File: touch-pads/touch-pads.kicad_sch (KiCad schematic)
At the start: 47 parts, among them J1 Conn_01x06_Pin, J2 Conn_01x06_Socket, J3 Conn_01x06_Pin, K1 Conn_01x01, K10 Conn_01x01, K11 Conn_01x01, K12 Conn_01x01, K13 Conn_01x01, K14 Conn_01x01, K15 Conn_01x01, K16 Conn_01x01, K17 Conn_01x01, K18 Conn_01x01, K19 Conn_01x01, K2 Conn_01x01, K20 Conn_01x01, K21 Conn_01x01, K22 Conn_01x01, K23 Conn_01x01, K24 Conn_01x01, K25 Conn_01x01, K26 Conn_01x01, K27 Conn_01x01, K28 Conn_01x01, K29 Conn_01x01, K3 Conn_01x01, K30 Conn_01x01, K31 Conn_01x01, K32 Conn_01x01, K4 Conn_01x01, K5 Conn_01x01, K6 Conn_01x01, K7 Conn_01x01, K8 Conn_01x01, K9 Conn_01x01, U10 CAP1188-1-CP-TR, U11 CAP1188-1-CP-TR, U8 CAP1188-1-CP-TR, U9 CAP1188-1-CP-TR

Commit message: small board
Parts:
- removed K10, K11, K12, K13, K14, K15, K16, K17, K18, K19, K20, K21, K22, K23, K24, K25, K26, K27, K28, K29, K30, K31, K32, K9: Conn_01x01, TouchKey:TouchKey_Standard, symbol Connector_Generic:Conn_01x01
- removed R16, R17, R18: 10k, Resistor_SMD:R_0805_2012Metric_Pad1.20x1.40mm_HandSolder, symbol Device:R
- removed R20: 120k, Resistor_SMD:R_0805_2012Metric_Pad1.20x1.40mm_HandSolder, symbol Device:R
- removed R21: 100k, Resistor_SMD:R_0805_2012Metric_Pad1.20x1.40mm_HandSolder, symbol Device:R
- removed R22: 82k, Resistor_SMD:R_0805_2012Metric_Pad1.20x1.40mm_HandSolder, symbol Device:R
- removed U10, U11, U9: CAP1188-1-CP-TR, CAP1188_1_CP_TR:QFN24_4X4MC_MCH, symbol CAP1188_1_CP_TR:CAP1188-1-CP-TR
- J1, J3: footprint (none) -> Connector_PinHeader_2.54mm:PinHeader_1x06_P2.54mm_Horizontal
- J2: footprint (none) -> Connector_PinSocket_2.54mm:PinSocket_1x06_P2.54mm_Horizontal
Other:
- moved on the sheet: J1, J2, J3, K1, K2, K3, K4, K5, K6, K7, K8, R15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

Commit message: large board
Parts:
- removed J1, J3: Conn_01x06_Pin, Connector_PinHeader_2.54mm:PinHeader_1x06_P2.54mm_Horizontal, symbol Connector:Conn_01x06_Pin
- added K10, K11, K12, K13, K14, K15, K16, K17, K18, K19, K20, K21, K22, K23, K24, K25, K26, K27, K28, K29, K30, K31, K32, K9: Conn_01x01, TouchKey:TouchKey_Standard, symbol Connector_Generic:Conn_01x01
- added R2, R5, R6: 10k, Resistor_SMD:R_0805_2012Metric_Pad1.20x1.40mm_HandSolder, symbol Device:R
- added R4: 100k, Resistor_SMD:R_0805_2012Metric_Pad1.20x1.40mm_HandSolder, symbol Device:R
- added R7: 120k, Resistor_SMD:R_0805_2012Metric_Pad1.20x1.40mm_HandSolder, symbol Device:R
- added R8: 82k, Resistor_SMD:R_0805_2012Metric_Pad1.20x1.40mm_HandSolder, symbol Device:R
- added U2, U3, U4: CAP1188-1-CP-TR, CAP1188_1_CP_TR:QFN24_4X4MC_MCH, symbol CAP1188_1_CP_TR:CAP1188-1-CP-TR
- J1: renamed from J2; footprint Connector_PinSocket_2.54mm:PinSocket_1x06_P2.54mm_Horizontal -> Connector_JST:JST_XH_B6B-XH-A_1x06_P2.50mm_Vertical
- renumbered R15 to R1, R19 to R3, U8 to U1
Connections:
- net +3.3V: now also J1.4 (Pin_4), U2.23 (VDD), U3.23 (VDD), U4.23 (VDD); no longer J1.5 (Pin_5)
- net ALERT: now also J1.6 (Pin_6), U2.13 (*ALERT/*BC_IRQ), U3.13 (*ALERT/*BC_IRQ), U4.13 (*ALERT/*BC_IRQ); no longer J1.1 (Pin_1)
- net GND: now also J1.5 (Pin_5), R2.1, R4.2, R5.1, R6.1, R7.2, R8.2, U2.1 (*SPI_CS), U2.10 (LED6), U2.11 (LED7), U2.12 (LED8), U2.25 (EPAD), U2.5 (LED1), U2.6 (LED2), U2.7 (LED3), U2.8 (LED4), U2.9 (LED5), U3.1 (*SPI_CS), U3.10 (LED6), U3.11 (LED7), U3.12 (LED8), U3.25 (EPAD), U3.5 (LED1), U3.6 (LED2), U3.7 (LED3), U3.8 (LED4), U3.9 (LED5), U4.1 (*SPI_CS), U4.10 (LED6), U4.11 (LED7), U4.12 (LED8), U4.25 (EPAD), U4.5 (LED1), U4.6 (LED2), U4.7 (LED3), U4.8 (LED4), U4.9 (LED5); no longer J1.6 (Pin_6)
- net RESET: now also J1.3 (Pin_3), U2.24 (RESET), U3.24 (RESET), U4.24 (RESET); no longer J1.2 (Pin_2)
- net SMCLK: now also J1.1 (Pin_1), U2.4 (SMCLK/BC_CLK/SPI_CLK), U3.4 (SMCLK/BC_CLK/SPI_CLK), U4.4 (SMCLK/BC_CLK/SPI_CLK); no longer J1.4 (Pin_4)
- net SMDATA: now also J1.2 (Pin_2), U2.3 (SMDATA/BC_DATA/SPI_MSIO/SPI_MISO), U3.3 (SMDATA/BC_DATA/SPI_MSIO/SPI_MISO), U4.3 (SMDATA/BC_DATA/SPI_MSIO/SPI_MISO); no longer J1.3 (Pin_3)
- new net: K19.1 (Pin_1), U2.20 (CS3)
- new net: K12.1 (Pin_1), U3.19 (CS4)
- new net: R6.2, U4.2 (WAKE/SPI_MOSI)
- new net: K13.1 (Pin_1), U3.18 (CS5)
- new net: K29.1 (Pin_1), U4.18 (CS5)
- new net: K25.1 (Pin_1), U4.22 (CS1)
- new net: K14.1 (Pin_1), U3.17 (CS6)
- new net: R7.1, U3.14 (ADDR_COMM)
- new net: K16.1 (Pin_1), U3.15 (CS8)
- new net: K15.1 (Pin_1), U3.16 (CS7)
- new net: R5.2, U3.2 (WAKE/SPI_MOSI)
- new net: K11.1 (Pin_1), U3.20 (CS3)
- new net: K10.1 (Pin_1), U3.21 (CS2)
- new net: K9.1 (Pin_1), U3.22 (CS1)
- new net: K21.1 (Pin_1), U2.18 (CS5)
- new net: R2.2, U2.2 (WAKE/SPI_MOSI)
- new net: K31.1 (Pin_1), U4.16 (CS7)
- new net: K23.1 (Pin_1), U2.16 (CS7)
- new net: K32.1 (Pin_1), U4.15 (CS8)
- new net: R8.1, U4.14 (ADDR_COMM)
- new net: K30.1 (Pin_1), U4.17 (CS6)
- new net: K28.1 (Pin_1), U4.19 (CS4)
- new net: K27.1 (Pin_1), U4.20 (CS3)
- new net: K26.1 (Pin_1), U4.21 (CS2)
- new net: K17.1 (Pin_1), U2.22 (CS1)
- new net: K22.1 (Pin_1), U2.17 (CS6)
- new net: R4.1, U2.14 (ADDR_COMM)
- new net: K24.1 (Pin_1), U2.15 (CS8)
- new net: K20.1 (Pin_1), U2.19 (CS4)
- new net: K18.1 (Pin_1), U2.21 (CS2)
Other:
- moved on the sheet: J1

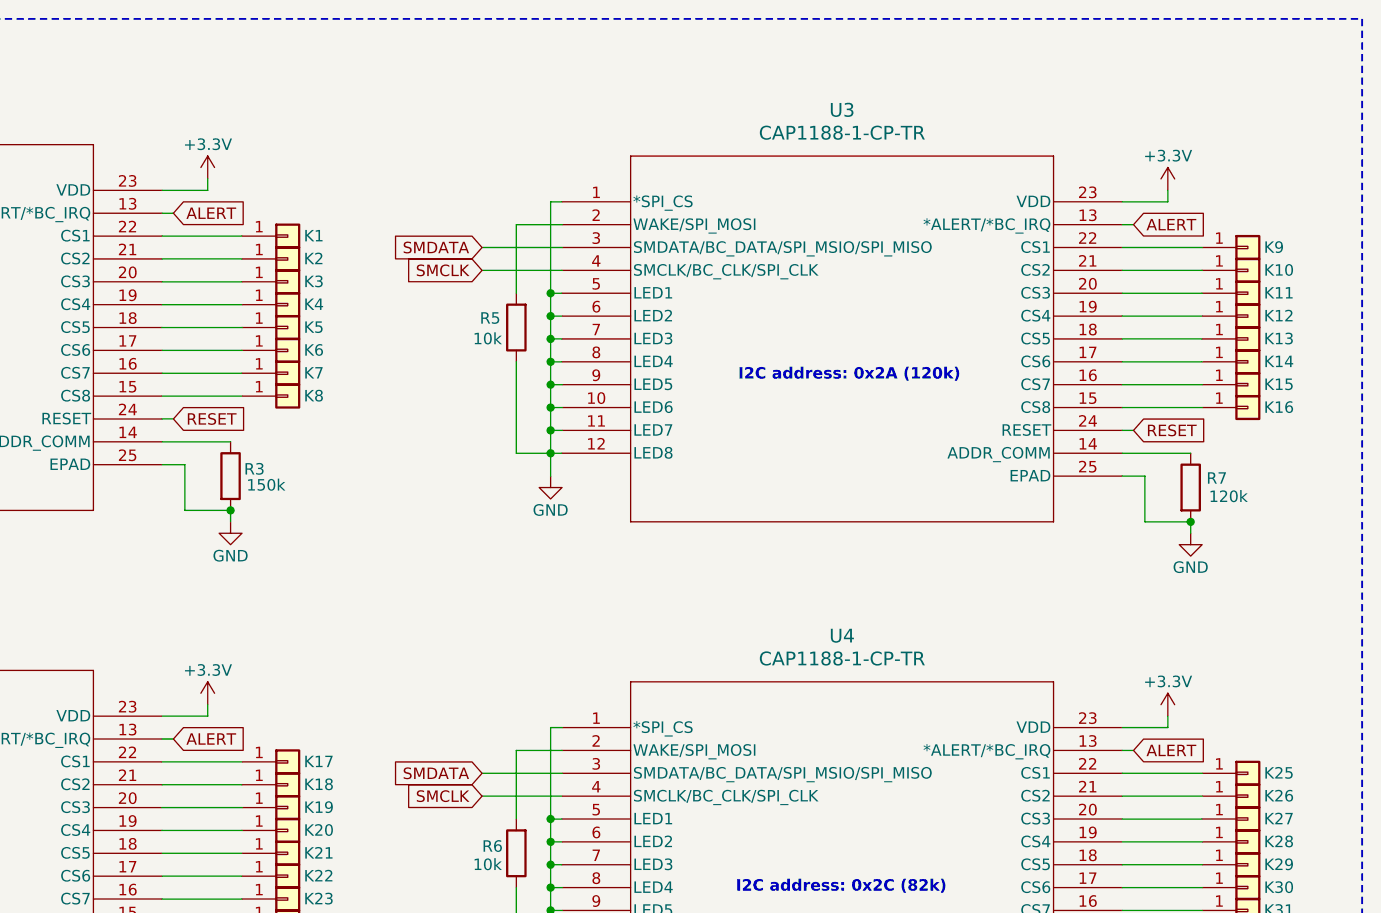
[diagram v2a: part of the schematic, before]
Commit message: add bypass caps
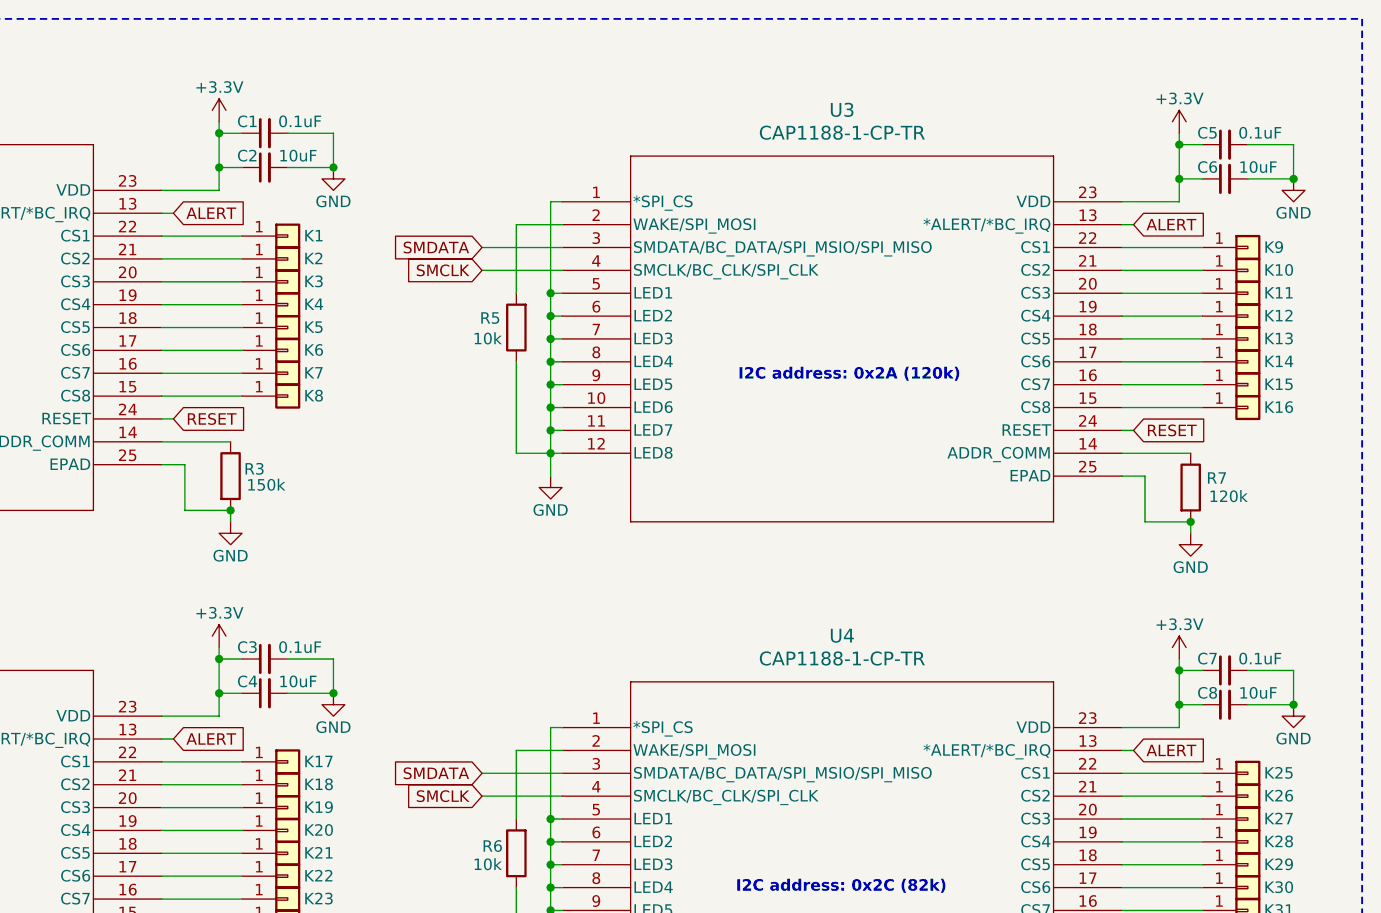
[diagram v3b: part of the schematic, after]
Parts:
- added C1, C3, C5, C7: 0.1uF, Capacitor_SMD:C_0805_2012Metric_Pad1.18x1.45mm_HandSolder, symbol Device:C_Small
- added C2, C4, C6, C8: 10uF, Capacitor_SMD:C_0805_2012Metric_Pad1.18x1.45mm_HandSolder, symbol Device:C_Small
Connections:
- net +3.3V: now also C1.1, C2.1, C3.1, C4.1, C5.1, C6.1, C7.1, C8.1
- net GND: now also C1.2, C2.2, C3.2, C4.2, C5.2, C6.2, C7.2, C8.2

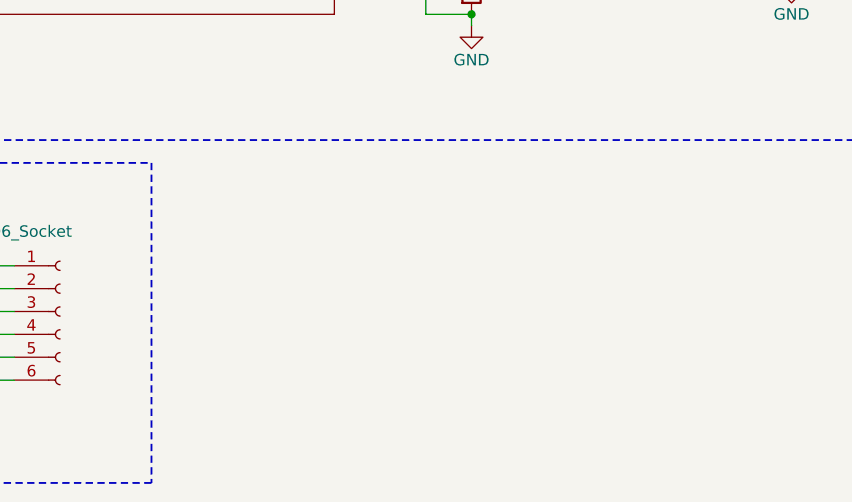
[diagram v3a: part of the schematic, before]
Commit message: mounting holes on schematic
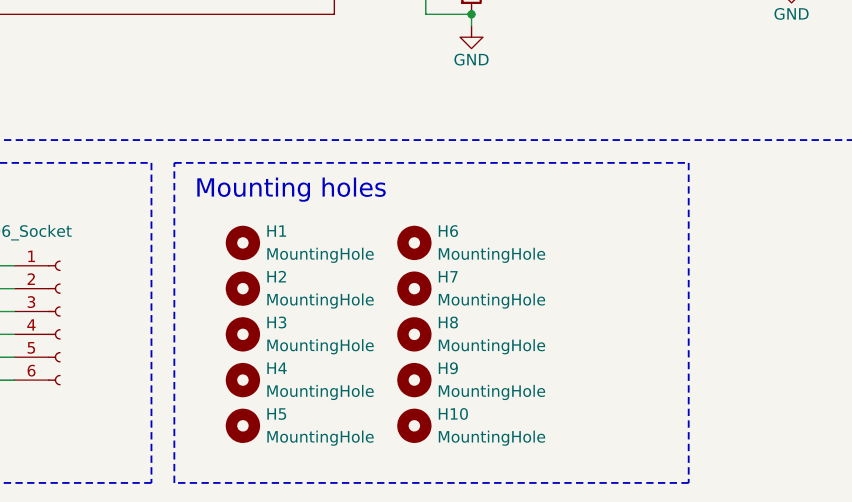
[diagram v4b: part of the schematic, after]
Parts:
- added H1, H10, H2, H3, H4, H5, H6, H7, H8, H9: MountingHole, MountingHole:MountingHole_3.2mm_M3, symbol Mechanical:MountingHole
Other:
- note added: "Mounting holes"
